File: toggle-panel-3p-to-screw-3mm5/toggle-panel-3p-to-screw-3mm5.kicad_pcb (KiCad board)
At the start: 2 copper layers, 14 x 16 mm, 2 parts, among them J1 Conn_01x03_Socket, SW1 SW_SPDT

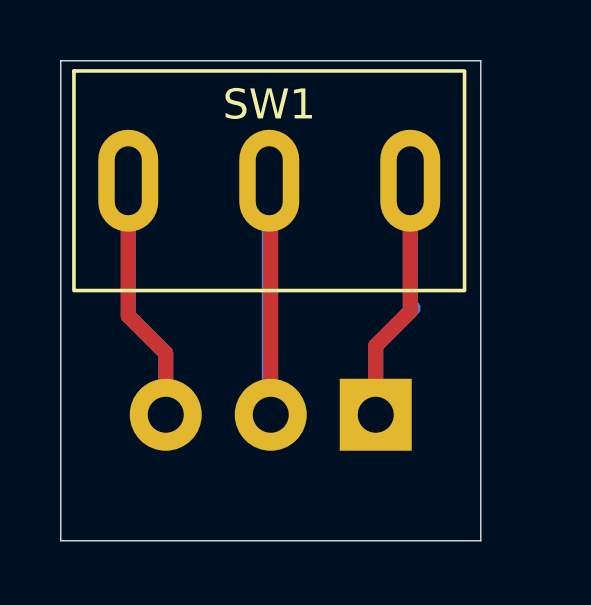
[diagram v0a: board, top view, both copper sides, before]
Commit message: Add single-board Gerbers for the 3-pin toggle panel adapter.
Export fabrication files for a single PCB, including copper, mask, silkscreen, paste, drills, and the manufacturing zip.
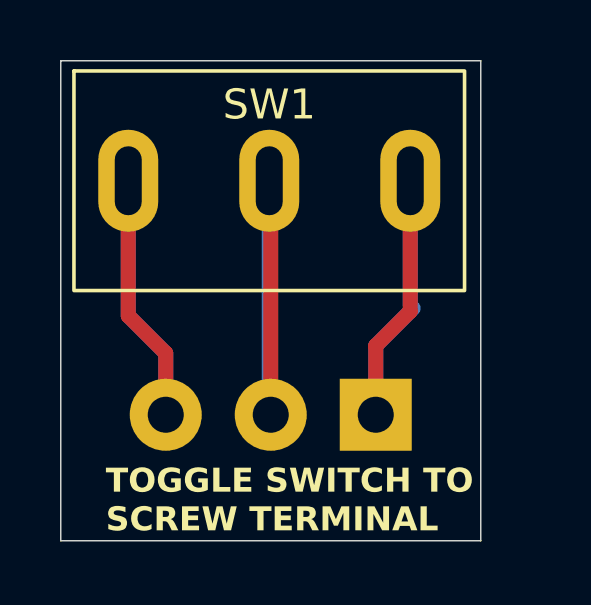
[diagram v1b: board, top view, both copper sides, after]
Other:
- board text added: "TOGGLE SWITCH TO SCREW TERMINAL"
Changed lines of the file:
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@@
   (gr_rect (start 100 100) (end 114 116)
     (stroke (width 0.05) (type default)) (fill none) (layer "Edge.Cuts"))
+  (gr_text "TOGGLE SWITCH TO\nSCREW TERMINAL" (at 101.5 115.75) (layer "F.SilkS")
+    (effects (font (size 0.8 0.8) (thickness 0.175) bold) (justify left bottom))
+  )
   (segment (start 111.65 104) (end 111.65 108.35) (width 0.5) (layer "F.Cu") (net 1))
   (segment (start 110.5 109.5) (end 110.5 111.8) (width 0.5) (layer "F.Cu") (net 1))
